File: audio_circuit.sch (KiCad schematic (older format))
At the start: 24 parts

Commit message: Changed BOM due to availability
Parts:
- C5, C6, C8: Mouser Best.Nr. 80-C0805C150J4HAUTO -> 710-885012007011
- RV1, RV2, RV3: value 10k -> 5k; Mouser Best.Nr. 72-TS53YL-10K -> 72-TS53YL-5K
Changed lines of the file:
@@
 P 3150 6050
 F 0 "RV3" V 3050 6050 50  0000 C CNN
-F 1 "10k" V 2950 6050 50  0000 C CNN
+F 1 "5k" V 2950 6050 50  0000 C CNN
 F 2 "Potentiometer_SMD:Potentiometer_Vishay_TS53YL_Vertical" H 3150 6050 50  0001 C CNN
 F 3 "~" H 3150 6050 50  0001 C CNN
-F 4 " 72-TS53YL-10K" H 300 50  50  0001 C CNN "Mouser Best.Nr."
+F 4 " 72-TS53YL-5K" H 300 50  50  0001 C CNN "Mouser Best.Nr."
 	1    3150 6050
 	0    1    -1   0
@@
 F 2 "Capacitor_SMD:C_0805_2012Metric_Pad1.15x1.40mm_HandSolder" H 3188 6450 50  0001 C CNN
 F 3 "~" H 3150 6600 50  0001 C CNN
-F 4 "80-C0805C150J4HAUTO" H 300 200 50  0001 C CNN "Mouser Best.Nr."
+F 4 "710-885012007011" H 300 200 50  0001 C CNN "Mouser Best.Nr."
 	1    3150 6600
 	1    0    0    -1
@@
 P 1100 4400
 F 0 "RV1" V 1000 4400 50  0000 C CNN
-F 1 "10k" V 900 4400 50  0000 C CNN
+F 1 "5k" V 900 4400 50  0000 C CNN
 F 2 "Potentiometer_SMD:Potentiometer_Vishay_TS53YL_Vertical" H 1100 4400 50  0001 C CNN
 F 3 "~" H 1100 4400 50  0001 C CNN
-F 4 " 72-TS53YL-10K" H -1750 -1600 50  0001 C CNN "Mouser Best.Nr."
+F 4 " 72-TS53YL-5K" H -1750 -1600 50  0001 C CNN "Mouser Best.Nr."
 	1    1100 4400
 	1    0    0    -1
@@
 P 2550 1950
 F 0 "RV2" V 2450 1950 50  0000 C CNN
-F 1 "10k" V 2350 1950 50  0000 C CNN
+F 1 "5k" V 2350 1950 50  0000 C CNN
 F 2 "Potentiometer_SMD:Potentiometer_Vishay_TS53YL_Vertical" H 2550 1950 50  0001 C CNN
 F 3 "~" H 2550 1950 50  0001 C CNN
-F 4 " 72-TS53YL-10K" H -300 -4050 50  0001 C CNN "Mouser Best.Nr."
+F 4 " 72-TS53YL-5K" H -300 -4050 50  0001 C CNN "Mouser Best.Nr."
 	1    2550 1950
 	1    0    0    -1
@@
 F 2 "Capacitor_SMD:C_0805_2012Metric_Pad1.15x1.40mm_HandSolder" H 3688 2200 50  0001 C CNN
 F 3 "~" H 3650 2350 50  0001 C CNN
-F 4 "80-C0805C150J4HAUTO" H 800 -4050 50  0001 C CNN "Mouser Best.Nr."
+F 4 "710-885012007011" H 800 -4050 50  0001 C CNN "Mouser Best.Nr."
 	1    3650 2350
 	1    0    0    -1
@@
 F 2 "Capacitor_SMD:C_0805_2012Metric_Pad1.15x1.40mm_HandSolder" H 2688 6450 50  0001 C CNN
 F 3 "~" H 2650 6600 50  0001 C CNN
-F 4 "80-C0805C150J4HAUTO" H -200 200 50  0001 C CNN "Mouser Best.Nr."
+F 4 "710-885012007011" H -200 200 50  0001 C CNN "Mouser Best.Nr."
 	1    2650 6600
 	1    0    0    -1

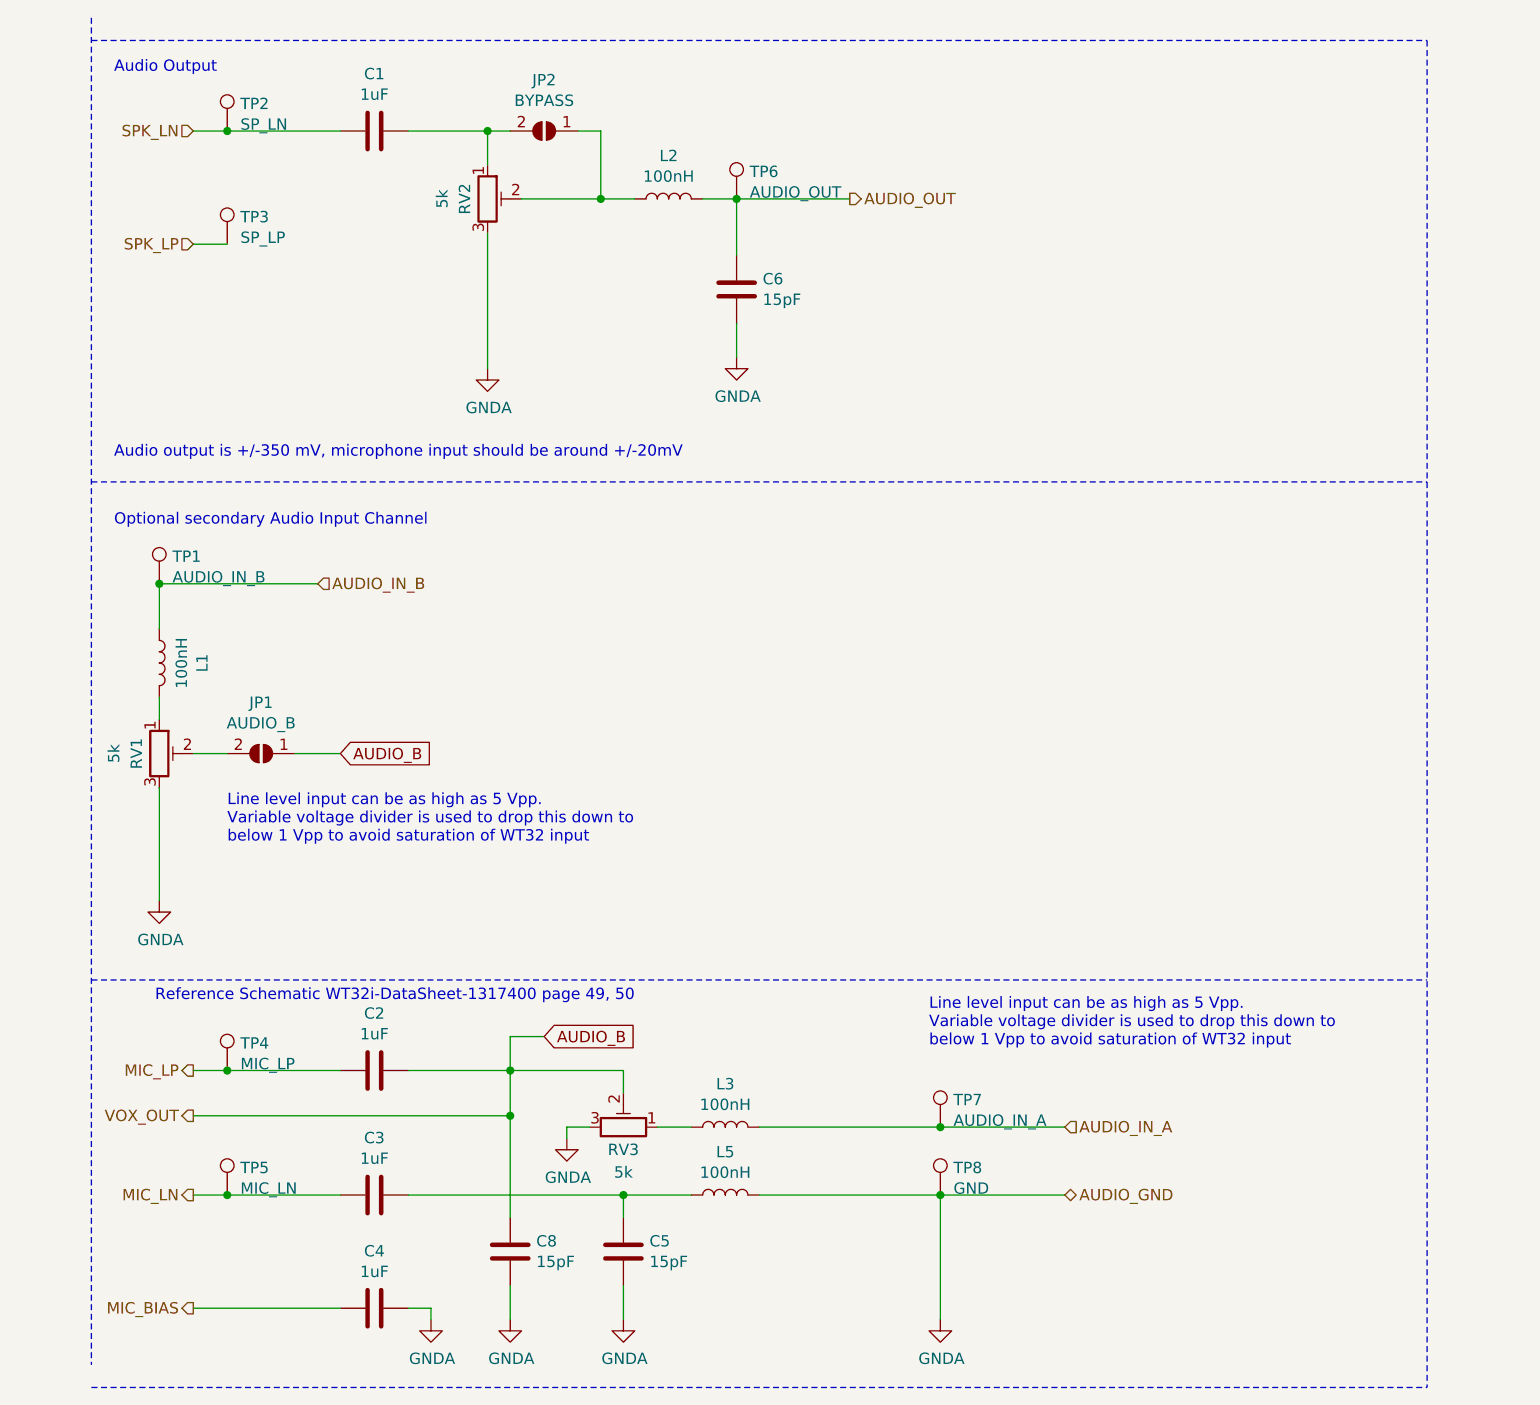
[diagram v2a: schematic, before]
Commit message: [#23] Remove AUDIO_IN_B
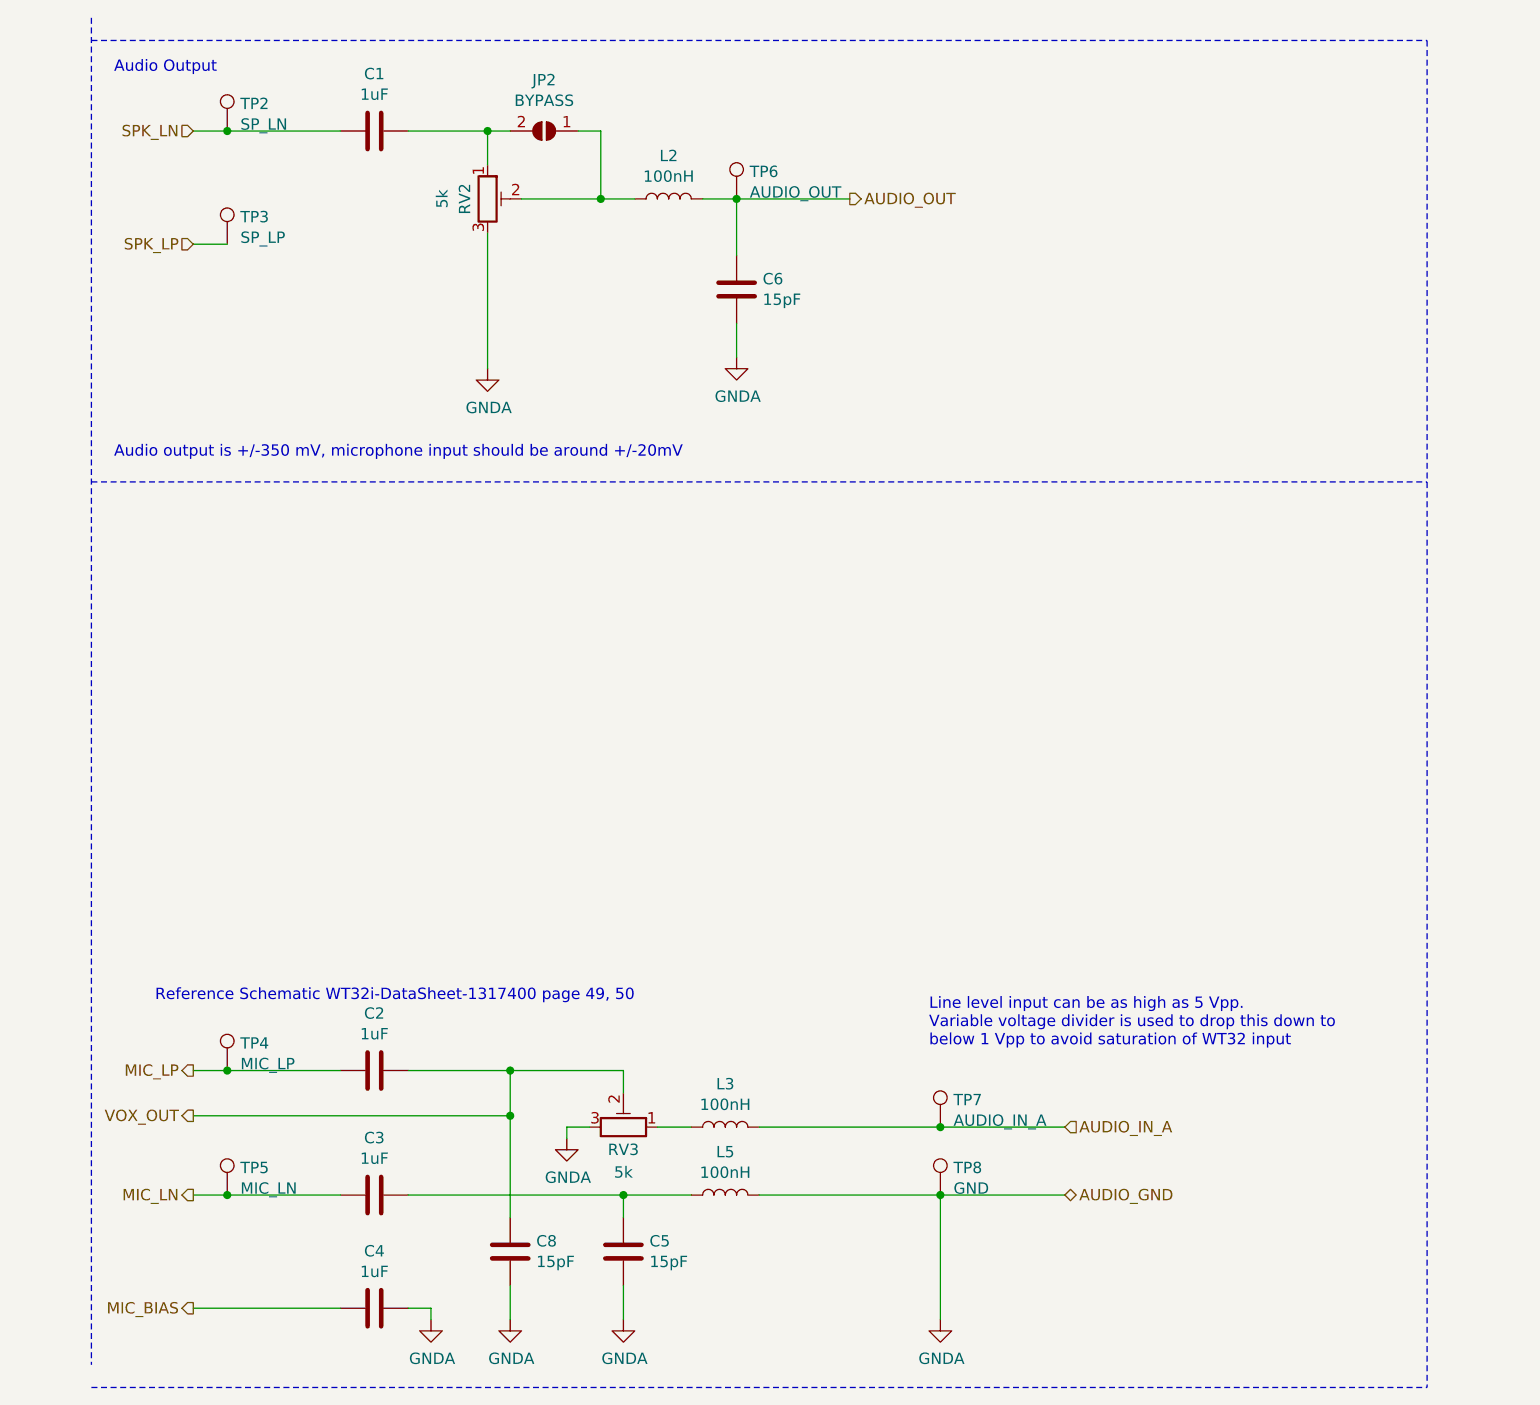
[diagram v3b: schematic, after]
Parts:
- removed JP1: AUDIO_B, Jumper:SolderJumper-2_P1.3mm_Open_TrianglePad1.0x1.5mm, symbol Jumper:SolderJumper_2_Open
- removed L1: 100nH, Inductor_SMD:L_0805_2012Metric_Pad1.15x1.40mm_HandSolder, symbol Device:L
- removed RV1: 5k, Potentiometer_SMD:Potentiometer_Vishay_TS53YL_Vertical, symbol Device:R_POT_TRIM
- removed TP1: AUDIO_IN_B, TestPoint:TestPoint_Pad_D1.5mm, symbol Connector:TestPoint
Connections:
- net AUDIO_B renamed VOX_OUT
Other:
- note removed: "Optional secondary Audio Input Channel"
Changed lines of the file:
@@
 Text Notes 4500 5700 0    50   ~ 0
 Line level input can be as high as 5 Vpp.\nVariable voltage divider is used to drop this down to\nbelow 1 Vpp to avoid saturation of WT32 input
-Text Notes 900  3400 0    50   ~ 0
-Optional secondary Audio Input Channel
 Wire Wire Line
 	2300 6850 2300 6900
@@
 Wire Notes Line
 	800  1150 800  7100
-Text HLabel 1800 3650 2    50   Input ~ 0
-AUDIO_IN_B
 Wire Notes Line
 	6700 1250 6700 7200
@@
 Wire Notes Line
 	800  7200 6700 7200
-Wire Notes Line
-	800  5400 6700 5400
 Wire Notes Line
 	800  3200 6700 3200
@@
 Wire Wire Line
 	3150 6750 3150 6900
-$Comp
-L Device:L L1
-U 1 1 5C7723BE
-P 1100 4000
-F 0 "L1" V 1290 4000 50  0000 C CNN
-F 1 "100nH" V 1199 4000 50  0000 C CNN
-F 2 "Inductor_SMD:L_0805_2012Metric_Pad1.15x1.40mm_HandSolder" H 1100 4000 50  0001 C CNN
-F 3 "~" H 1100 4000 50  0001 C CNN
-F 4 "810-MLF2012DR10MT000" H -2200 -2000 50  0001 C CNN "Mouser Best.Nr."
-	1    1100 4000
-	1    0    0    -1
-$EndComp
-$Comp
-L Device:R_POT_TRIM RV1
-U 1 1 5C7723C7
-P 1100 4400
-F 0 "RV1" V 1000 4400 50  0000 C CNN
-F 1 "5k" V 900 4400 50  0000 C CNN
-F 2 "Potentiometer_SMD:Potentiometer_Vishay_TS53YL_Vertical" H 1100 4400 50  0001 C CNN
-F 3 "~" H 1100 4400 50  0001 C CNN
-F 4 " 72-TS53YL-5K" H -1750 -1600 50  0001 C CNN "Mouser Best.Nr."
-	1    1100 4400
-	1    0    0    -1
-$EndComp
-$Comp
-L power:GNDA #PWR014
-U 1 1 5C7723EC
-P 1100 5050
-F 0 "#PWR014" H 1100 4800 50  0001 C CNN
-F 1 "GNDA" H 1105 4877 50  0000 C CNN
-F 2 "" H 1100 5050 50  0001 C CNN
-F 3 "" H 1100 5050 50  0001 C CNN
-	1    1100 5050
-	1    0    0    -1
-$EndComp
 Wire Wire Line
 	4550 6350 5100 6350
-$Comp
-L Jumper:SolderJumper_2_Open JP1
-U 1 1 5C773465
-P 1550 4400
-F 0 "JP1" H 1550 4175 50  0000 C CNN
-F 1 "AUDIO_B" H 1550 4266 50  0000 C CNN
-F 2 "Jumper:SolderJumper-2_P1.3mm_Open_TrianglePad1.0x1.5mm" H 1550 4400 50  0001 C CNN
-F 3 "~" H 1550 4400 50  0001 C CNN
-F 4 "-" H 0   0   50  0001 C CNN "Mouser Best.Nr."
-	1    1550 4400
-	-1   0    0    1
-$EndComp
-Wire Wire Line
-	1100 3650 1100 3850
-Wire Wire Line
-	1100 4150 1100 4250
-Wire Wire Line
-	1250 4400 1400 4400
-Text GLabel 1900 4400 2    50   Input ~ 0
-AUDIO_B
-Wire Wire Line
-	1700 4400 1900 4400
-Text Notes 1400 4800 0    50   ~ 0
-Line level input can be as high as 5 Vpp.\nVariable voltage divider is used to drop this down to\nbelow 1 Vpp to avoid saturation of WT32 input
 $Comp
 L Device:C C1
@@
 Wire Wire Line
 	1400 6350 1900 6350
-$Comp
-L Connector:TestPoint TP1
-U 1 1 5C77A4DC
-P 1100 3650
-F 0 "TP1" H 1158 3770 50  0000 L CNN
-F 1 "AUDIO_IN_B" H 1158 3679 50  0000 L CNN
-F 2 "TestPoint:TestPoint_Pad_D1.5mm" H 1300 3650 50  0001 C CNN
-F 3 "~" H 1300 3650 50  0001 C CNN
-F 4 "-" H 0   0   50  0001 C CNN "Mouser Best.Nr."
-	1    1100 3650
-	1    0    0    -1
-$EndComp
-Connection ~ 1100 3650
 Text Notes 900  1400 0    50   ~ 0
 Audio Output
@@
 Wire Wire Line
 	2200 1650 2550 1650
-Wire Wire Line
-	1100 3650 1800 3650
 Text HLabel 1250 2150 0    50   Input ~ 0
 SPK_LP
@@
 	3750 6350 4550 6350
 Wire Wire Line
-	2200 5800 2650 5800
-Wire Wire Line
 	3450 6050 3300 6050
 Wire Wire Line
@@
 Wire Wire Line
 	3150 6350 3450 6350
-Connection ~ 2650 5800
-Wire Wire Line
-	2650 5800 3150 5800
-Wire Wire Line
-	1100 4550 1100 5050
-Text GLabel 2800 5650 2    50   Input ~ 0
-AUDIO_B
 Wire Wire Line
 	2650 6450 2650 6000
-Wire Wire Line
-	2650 5800 2650 5650
-Wire Wire Line
-	2650 5650 2800 5650
 Text HLabel 1250 6000 0    50   Output ~ 0
 VOX_OUT
 Wire Wire Line
 	1250 6000 2650 6000
+Wire Wire Line
+	2200 5800 2650 5800
+Wire Wire Line
+	2650 6000 2650 5800
 Connection ~ 2650 6000
-Wire Wire Line
-	2650 6000 2650 5800
+Connection ~ 2650 5800
+Wire Wire Line
+	2650 5800 3150 5800
 $EndSCHEMATC

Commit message: Audio Rework in Schematic [#21]
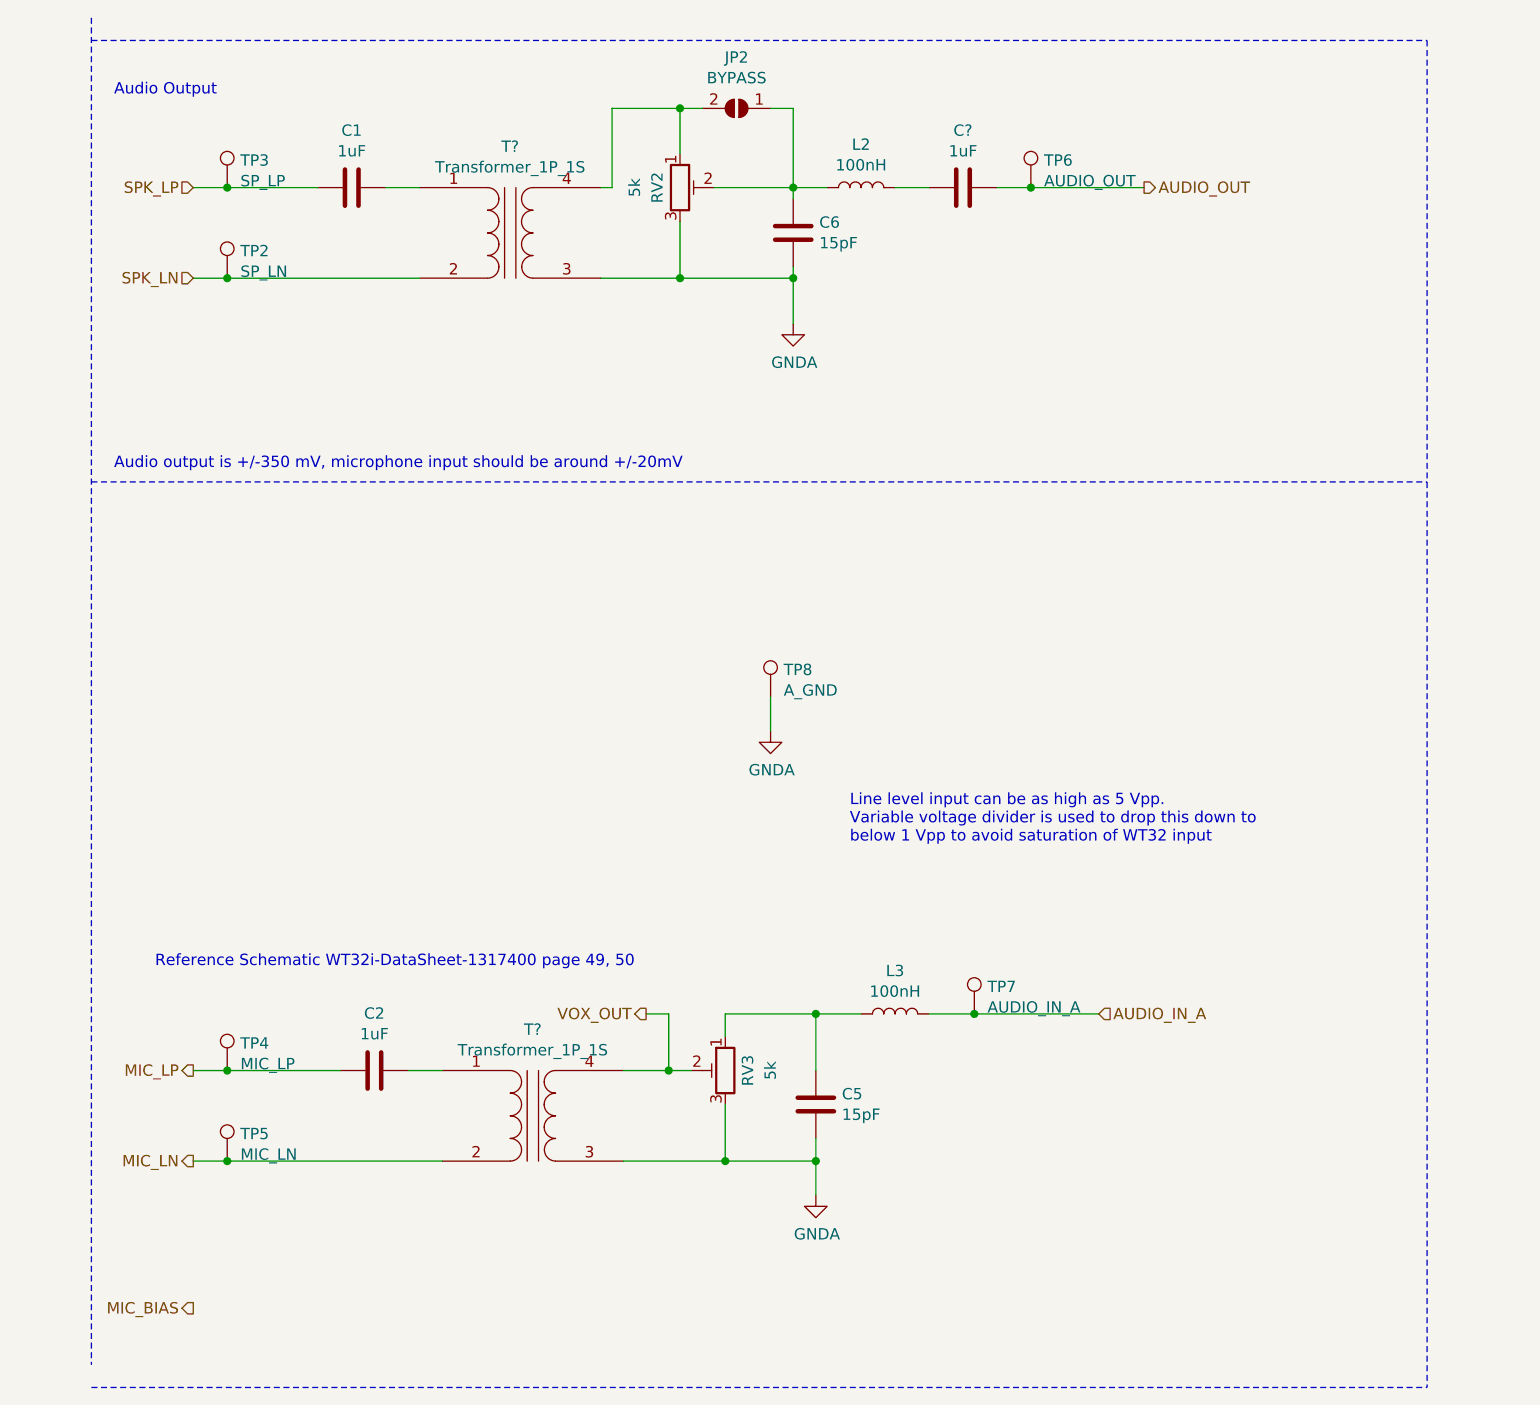
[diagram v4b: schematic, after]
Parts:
- removed C3, C4: 1uF, Capacitor_SMD:C_0805_2012Metric_Pad1.15x1.40mm_HandSolder, symbol Device:C
- removed C8: 15pF, Capacitor_SMD:C_0805_2012Metric_Pad1.15x1.40mm_HandSolder, symbol Device:C
- removed L5: 100nH, Inductor_SMD:L_0805_2012Metric_Pad1.15x1.40mm_HandSolder, symbol Device:L
- added C?: 1uF, Capacitor_SMD:C_0805_2012Metric_Pad1.15x1.40mm_HandSolder, symbol Device:C
- added T? (x2): Transformer_1P_1S, symbol Device:Transformer_1P_1S
- TP8: value GND -> A_GND
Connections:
- net AUDIO_OUT: now also C?.1; no longer C6.1, L2.2
- net GNDA: now also T?.3 (SA), T?.3 (SA)
- net MIC_LN: now also T?.2 (AB)
- net SPK_LN: now also T?.2 (AB); no longer C1.2
- net SPK_LP: now also C1.2
- net VOX_OUT: now also T?.4 (SB); no longer C2.1
- net at C5.1: now also L3.1, RV3.1
- net at JP2.2 (B), RV2.1: now also T?.4 (SB); no longer C1.1
- net at JP2.1 (A), L2.1, RV2.2: now also C6.1
- new net: C2.1, T?.1 (AA)
- new net: C1.1, T?.1 (AA)
- new net: C?.2, L2.2
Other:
- moved on the sheet: C1, C5, C6, JP2, L2, L3, RV2, RV3, TP2, TP3, TP5, TP6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
